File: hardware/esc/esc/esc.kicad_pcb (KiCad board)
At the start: 4 copper layers, 40.2 x 42.5 mm, 189 parts, among them J1 JST SH 1.0mm, Q1 Q_NMOS, Q10 Q_NMOS, Q11 Q_NMOS, Q12 Q_NMOS, Q13 Q_NMOS, Q14 Q_NMOS, Q15 Q_NMOS, Q16 Q_NMOS, Q17 Q_NMOS, Q18 Q_NMOS, Q19 Q_NMOS, Q2 Q_NMOS, Q20 Q_NMOS, Q21 Q_NMOS, Q22 Q_NMOS, Q23 Q_NMOS, Q24 Q_NMOS, Q3 Q_NMOS, Q4 Q_NMOS, Q5 Q_NMOS, Q6 Q_NMOS, Q7 Q_NMOS, Q8 Q_NMOS, Q9 Q_NMOS, U1 NSG2065Q, U10 TLV76733DRVR, U11 LMR51420YDDCR, U2 AT32F421G8U7, U3 INA180B2, U4 AT32F421G8U7, U5 NSG2065Q, U6 AT32F421G8U7, U7 NSG2065Q, U8 AT32F421G8U7, U9 NSG2065Q

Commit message: ESC Layout try 1
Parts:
- C15, C16, C17, C28, C29, C30, C31, C4, C42, C43, C44, C45, C5, C56, C57, C58, C59, C6, C60, C7, FB1, FB2, FB3, FB4, R18, R19, R22, R23, R25, R26, R42, R43, R45, R46, R62, R63, R65, R66, R7, R8, TP1, TP2, TP3, TP4, TP5, TP6, TP7, TP8, U1, U10, U2, U4, U5, U6, U7, U8, U9: moved to B.Cu
- moved U10 111.7 mm to (40.1, 38.9), turned to 180 degrees
- moved C60 109.1 mm to (41.9, 33.4)
- moved C59 108.2 mm to (41.9, 35.4)
- moved U2 108.1 mm to (32.2, 27.9), turned to 90 degrees
- moved R19 108.0 mm to (26.4, 23.3), turned to -90 degrees
- moved R20 107.7 mm to (32.1, 34.1), turned to -90 degrees
- moved R8 106.8 mm to (35.4, 27.4), turned to -90 degrees
- moved C57 106.4 mm to (39.3, 36.2), turned to 90 degrees
- moved R18 105.4 mm to (27.9, 23.3), turned to 90 degrees
- moved D1 104.7 mm to (34.2, 33.7)
- moved C58 104.1 mm to (41.9, 37.1)
- moved TP1 102.0 mm to (35.0, 25.0), turned to 180 degrees
- moved TP2 100.8 mm to (35.1, 30.7), turned to 180 degrees
- moved C6 100.5 mm to (29.5, 23.3), turned to 90 degrees
- moved C7 100.3 mm to (31.0, 23.3), turned to 90 degrees
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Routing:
- net +BATT: track 135.0 -> 50.7 mm, vias 8 -> 0
- net GND: track 128.2 -> 93.1 mm, vias 16 -> 0
- net /CURR_SENSE: track 26.0 -> 0.00 mm, vias 1 -> 0
- net /ESC2/FloatB: track 26.3 -> 3.16 mm, vias 1 -> 0
- net /VBAT: track 21.1 -> 0.00 mm, vias 1 -> 0
- net +3.3V: track 0.00 -> 17.1 mm
- net /ESC1/FloatB: track 19.2 -> 3.18 mm, vias 1 -> 0
- net /ESC1/FloatC: track 19.0 -> 2.99 mm, vias 1 -> 0
- net /ESC4/FloatB: track 18.2 -> 2.83 mm, vias 1 -> 0
- net /ESC3/FloatB: track 19.0 -> 4.14 mm
- net /ESC4/FloatA: track 17.9 -> 3.18 mm, vias 1 -> 0
- net /ESC3/FloatC: track 23.6 -> 11.1 mm
- net Net-(Q1-PadG): track 12.2 -> 0.04 mm, vias 2 -> 0
- net Net-(Q3-PadG): track 12.2 -> 0.00 mm, vias 2 -> 0
- net Net-(Q5-PadG): track 12.1 -> 0.00 mm, vias 2 -> 0
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
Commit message: journal for 2nd april
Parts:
- moved FB4 0.60 mm to (47.7, 38.3)
- moved R65 0.60 mm to (44.4, 38.3)
- moved C45 0.60 mm to (45.9, 38.3)
- moved R46 0.05 mm to (36.4, 27.4)
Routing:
- net /CURR_SENSE: track 0.00 -> 34.8 mm, vias 0 -> 2
- net +3.3V: track 17.1 -> 47.0 mm, vias 0 -> 1
- net Net-(Q9-PadG): track 0.00 -> 20.7 mm
- net Net-(Q3-PadG): track 0.00 -> 20.4 mm
- net /ESC4/FloatA: track 3.18 -> 22.3 mm
- net Net-(Q7-PadG): track 0.00 -> 15.8 mm, vias 0 -> 2
- net /VBAT: track 0.00 -> 15.6 mm
- net Net-(Q5-PadG): track 0.00 -> 14.5 mm
- net Net-(Q11-PadG): track 0.00 -> 14.4 mm
- net +8V: track 7.09 -> 20.7 mm
- net Net-(Q13-PadG): track 0.00 -> 13.3 mm
- net /ESC4/FloatB: track 2.83 -> 15.9 mm
- net Net-(Q1-PadG): track 0.04 -> 12.8 mm, vias 0 -> 2
- net /ESC2/VOLT_SENSE: track 0.00 -> 12.3 mm
- net Net-(Q17-PadG): track 0.00 -> 11.4 mm, vias 0 -> 2
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
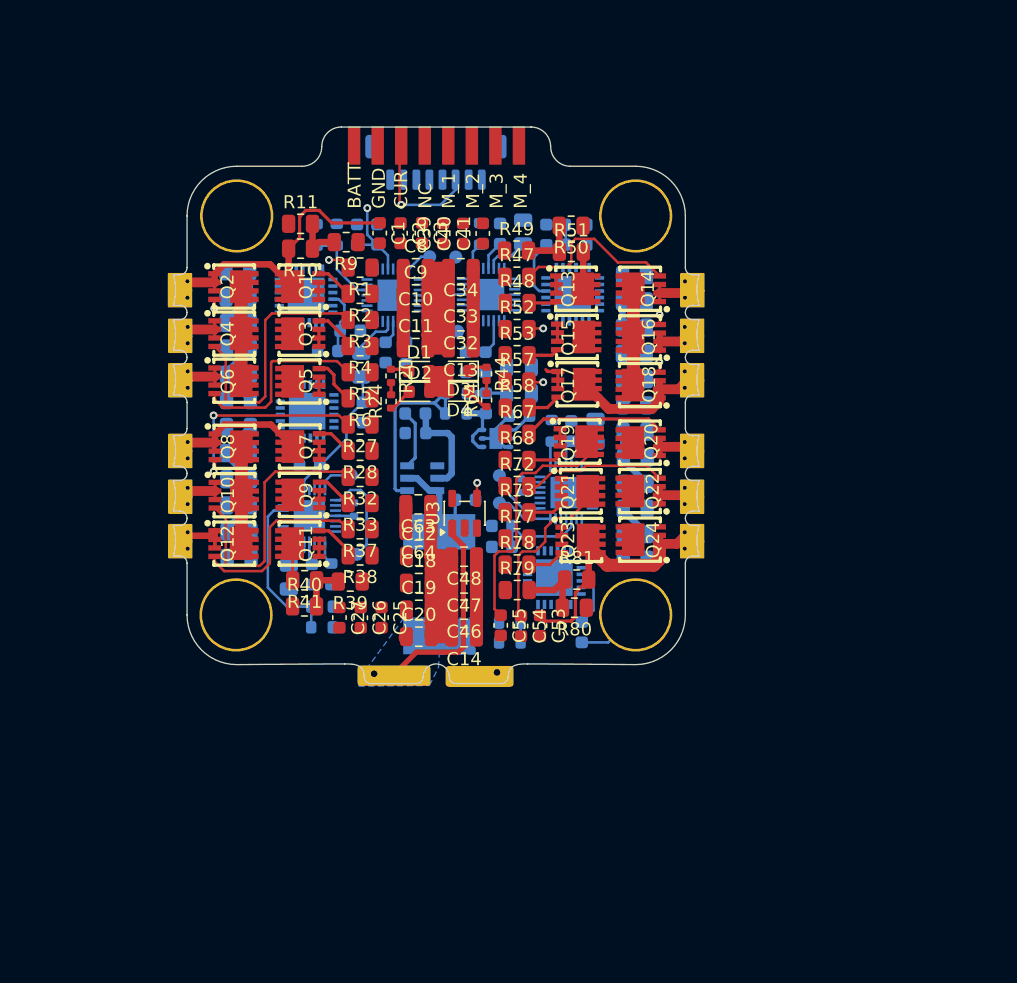
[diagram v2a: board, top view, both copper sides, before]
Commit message: redo layout and new board outline
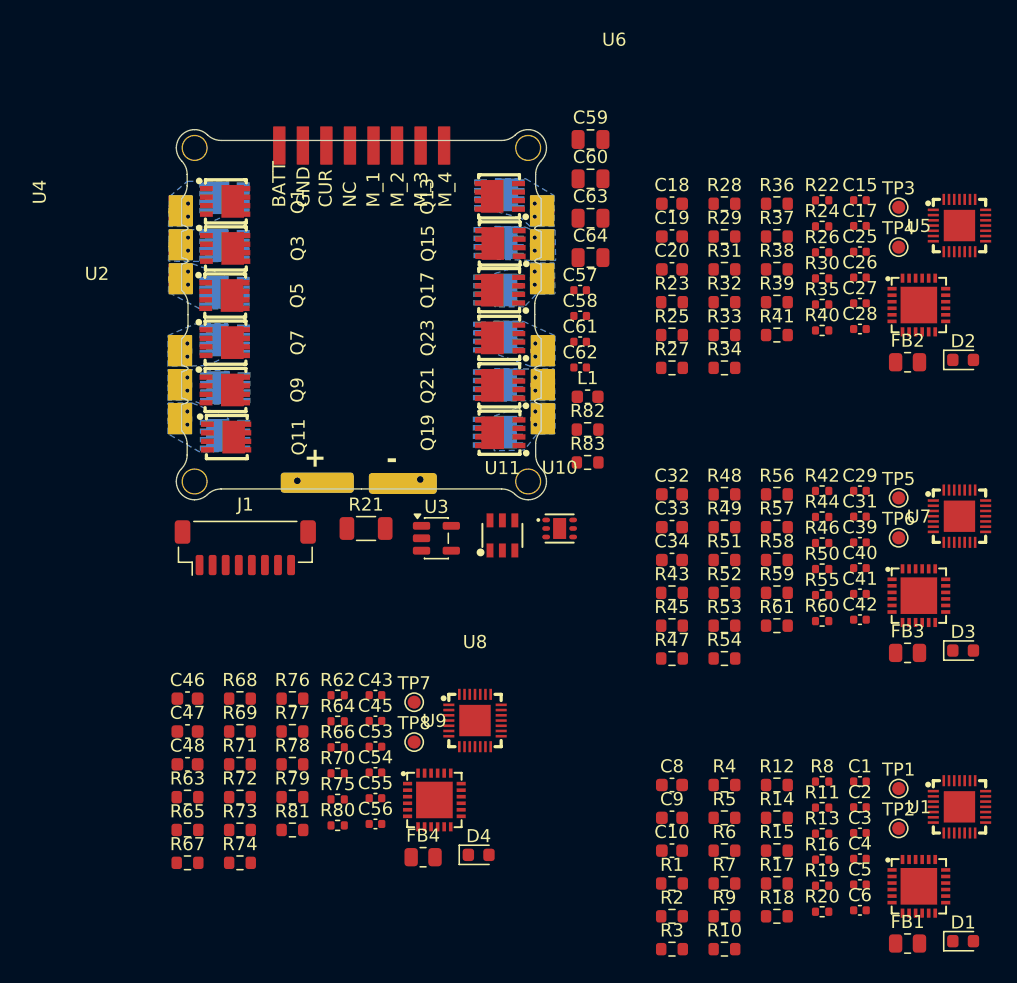
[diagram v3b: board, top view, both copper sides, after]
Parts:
- removed C11, C12, C13, C14: 22uF, Capacitor_SMD:C_0805_2012Metric
- removed C16, C30, C44, C7: 100nF, Capacitor_SMD:C_0603_1608Metric
- C1, C2, C25, C26, C27, C3, C39, C40, C41, C53, C54, C55: footprint Capacitor_SMD:C_0603_1608Metric -> Capacitor_SMD:C_0402_1005Metric
- C10, C18, C19, C20, C32, C33, C34, C46, C47, C48, C8, C9: value 22uF -> 10uF; footprint Capacitor_SMD:C_0805_2012Metric -> Capacitor_SMD:C_0603_1608Metric
- C15, C17, C28, C29, C31, C4, C42, C43, C45, C5, C56, C57, C58, C6, C61, C62: footprint Capacitor_SMD:C_0603_1608Metric -> Capacitor_SMD:C_0402_1005Metric; moved to F.Cu
- C59, C60, FB1, FB2, FB3, FB4, J1, L1, R18, R23, R25, R26, R43, R45, R46, R63, R65, R66, R7, R8, R82, R83, TP1, TP2, TP3, TP4, TP5, TP6, TP7, TP8, U1, U10, U11, U2, U4, U5, U6, U7, U8, U9: moved to F.Cu
- Q10, Q12, Q14, Q16, Q18, Q2, Q20, Q22, Q24, Q4, Q6, Q8: moved to B.Cu
- R1, R10, R2, R27, R28, R3, R32, R33, R37, R38, R39, R4, R41, R47, R48, R49, R5, R51, R52, R53, R57, R58, R6, R67, R68, R72, R73, R77, R78, R79, R81, R9: footprint Resistor_SMD:R_0805_2012Metric -> Resistor_SMD:R_0603_1608Metric
- R11, R40, R50, R80: footprint Resistor_SMD:R_0805_2012Metric -> Resistor_SMD:R_0402_1005Metric
- R12, R14, R15, R17, R29, R31, R34, R36, R54, R56, R59, R61, R69, R71, R74, R76: footprint Resistor_SMD:R_0805_2012Metric -> Resistor_SMD:R_0603_1608Metric; moved to F.Cu
- R13, R16, R30, R35, R55, R60, R70, R75: footprint Resistor_SMD:R_0805_2012Metric -> Resistor_SMD:R_0402_1005Metric; moved to F.Cu
- R19, R22, R42, R62: footprint Resistor_SMD:R_0603_1608Metric -> Resistor_SMD:R_0402_1005Metric; moved to F.Cu
- R21: footprint 3920:RES_3920R_1L00x_BRN -> Resistor_SMD:R_1206_3216Metric; moved to F.Cu
- moved U1 65.1 mm to (72.4, 73.1), turned to 0 degrees
- moved C6 64.4 mm to (67.9, 74.9), turned to 0 degrees
- moved R19 63.0 mm to (65.0, 73.1), turned to 0 degrees
- moved R10 62.6 mm to (57.6, 77.9), turned to 0 degrees
- moved R18 62.0 mm to (61.6, 75.4), turned to 0 degrees
- moved R13 62.0 mm to (65.0, 69.1)
- moved FB1 60.8 mm to (71.6, 77.5), turned to 0 degrees
- moved D1 60.3 mm to (75.8, 77.3)
- moved R11 59.9 mm to (65.0, 67.1)
- moved R9 59.1 mm to (57.6, 75.4), turned to 0 degrees
- moved U2 58.3 mm to (75.5, 67.0), turned to 0 degrees
- moved R17 58.0 mm to (61.6, 72.9), turned to 0 degrees
- moved R14 57.3 mm to (61.6, 67.9), turned to 0 degrees
- moved R16 56.8 mm to (65.0, 71.1)
- moved C3 56.8 mm to (67.9, 69.0), turned to 0 degrees
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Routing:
- net GND: track 97.4 -> 0.00 mm
- net +BATT: track 50.7 -> 0.00 mm
- net +3.3V: track 47.0 -> 0.00 mm, vias 1 -> 0
- net /CURR_SENSE: track 34.8 -> 0.00 mm, vias 2 -> 0
- net /ESC1/FloatA: track 23.2 -> 0.00 mm
- net /ESC4/FloatA: track 22.3 -> 0.00 mm
- net /ESC4/FloatC: track 21.1 -> 0.00 mm
- net Net-(Q9-PadG): track 20.7 -> 0.00 mm
- net +8V: track 20.7 -> 0.00 mm
- net Net-(Q3-PadG): track 20.4 -> 0.00 mm
- net /ESC4/FloatB: track 15.9 -> 0.00 mm
- net Net-(Q7-PadG): track 15.8 -> 0.00 mm, vias 2 -> 0
- net /VBAT: track 15.6 -> 0.00 mm
- net Net-(Q5-PadG): track 14.5 -> 0.00 mm
- net Net-(Q11-PadG): track 14.4 -> 0.00 mm
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- added copper zone on B.Cu, net /ESC1/FloatA
- added copper zone on B.Cu, net /ESC1/FloatB
- added copper zone on B.Cu, net /ESC1/FloatC
- added copper zone on B.Cu, net /ESC2/FloatA
- added copper zone on B.Cu, net /ESC2/FloatB
- added copper zone on B.Cu, net /ESC2/FloatC
- added copper zone on B.Cu, net /ESC3/FloatA
- added copper zone on B.Cu, net /ESC3/FloatB
- added copper zone on B.Cu, net /ESC3/FloatC
- added copper zone on B.Cu, net /ESC4/FloatA
- added copper zone on B.Cu, net /ESC4/FloatB
- added copper zone on B.Cu, net /ESC4/FloatC
- removed copper zone on B.Cu, net /VBAT
- removed copper zone on In1.Cu, net GND
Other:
- board size 40.2 x 42.5 mm -> 28.3 x 28.3 mm

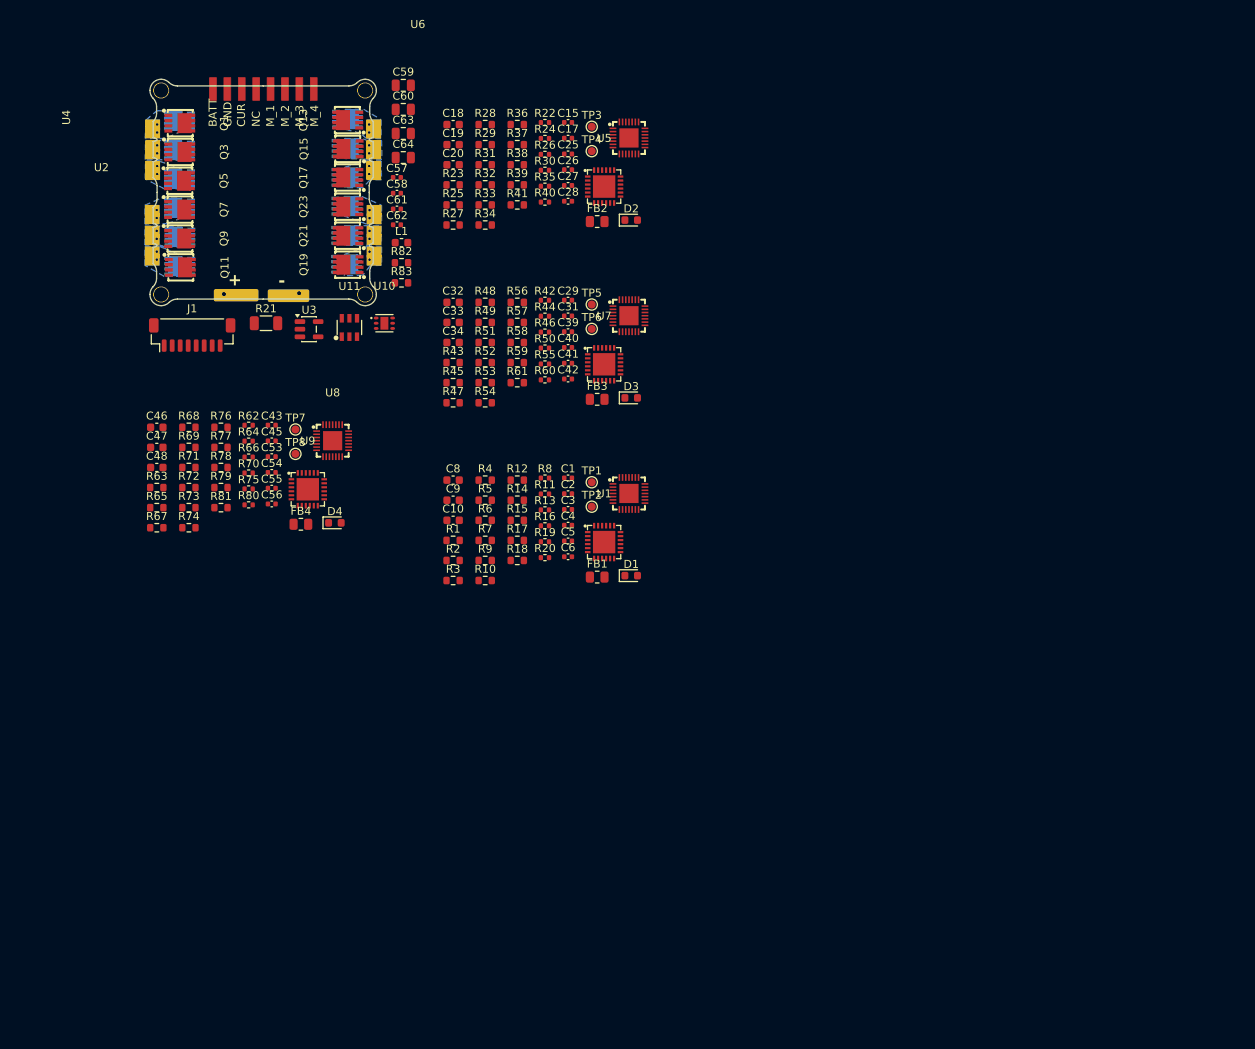
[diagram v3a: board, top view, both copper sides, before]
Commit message: board pcb + res arrays
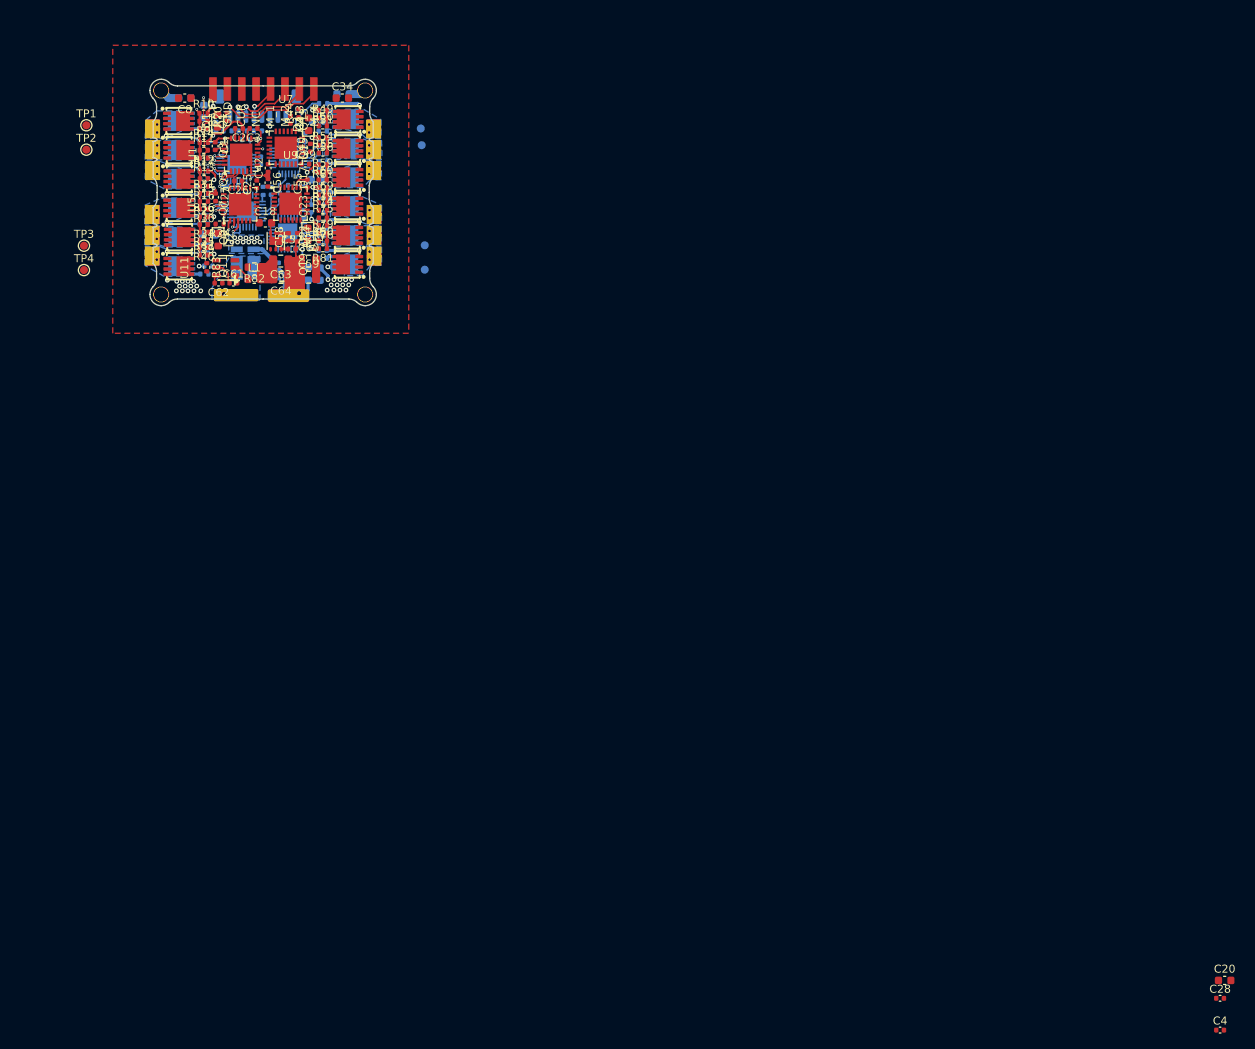
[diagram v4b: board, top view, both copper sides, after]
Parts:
- removed FB1, FB2, FB3, FB4: FerriteBead_Small, Resistor_SMD:R_0805_2012Metric
- removed R18, R23, R63: 10k, Resistor_SMD:R_0603_1608Metric
- removed R19, R22, R62: 100k, Resistor_SMD:R_0402_1005Metric
- C10, C15, C17, C19, C29, C31, C32, C33, C43, C45, C46, C47, C48, C5, C53, C54, C6, C9, J1, R26, R42, R46, R66, R8, TP5, TP6, TP7, TP8, U2, U3, U4, U6, U8: moved to B.Cu
- R1, R2, R27, R28, R3, R32, R33, R37, R38, R4, R47, R48, R5, R52, R53, R57, R58, R6, R67, R68, R72, R73, R77, R78: value 20R -> 22R; footprint Resistor_SMD:R_0603_1608Metric -> Resistor_SMD:R_0402_1005Metric; moved to B.Cu
- R10, R12, R14, R15, R17, R29, R31, R34, R36, R39, R41, R49, R51, R54, R56, R59, R61, R69, R71, R74, R76, R79, R81, R83, R9: footprint Resistor_SMD:R_0603_1608Metric -> Resistor_SMD:R_0402_1005Metric
- R21: value 0.4mR -> 0.5m; footprint Resistor_SMD:R_1206_3216Metric -> bvn-z-r0005-1.0:BVNZR000510; moved to B.Cu
- R25, R43, R45, R65, R7: footprint Resistor_SMD:R_0603_1608Metric -> Resistor_SMD:R_0402_1005Metric; moved to B.Cu
- moved C20 140.3 mm to (150.0, 127.9)
- moved C28 128.7 mm to (149.4, 130.1)
- moved C4 103.1 mm to (149.4, 134.1)
- moved TP1 77.3 mm to (7.70, 21.0)
- moved TP2 77.3 mm to (7.70, 24.1)
- moved D1 76.8 mm to (24.1, 20.4), turned to 90 degrees
- moved R10 68.2 mm to (22.4, 19.5)
- moved R20 67.9 mm to (25.3, 19.9), turned to 90 degrees
- moved U1 66.4 mm to (27.1, 24.7), turned to 90 degrees
- moved C6 65.6 mm to (22.4, 27.7), turned to 180 degrees
- moved R9 65.2 mm to (22.4, 20.5), turned to 180 degrees
- moved TP3 65.2 mm to (7.40, 36.0)
- moved TP4 65.2 mm to (7.40, 39.1)
- moved U2 64.0 mm to (26.5, 25.9), turned to 180 degrees
- moved C10 62.5 mm to (20.0, 17.6), turned to 180 degrees
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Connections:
- U2 pad 12: /ESC1/VOLT_SENSE -> unconnected-(U2-PA6-Pad12)
- U2 pad 5: Net-(U2-VDDA) -> +3.3V
- U4 pad 12: /ESC2/VOLT_SENSE -> unconnected-(U4-PA6-Pad12)
- U4 pad 5: Net-(U4-VDDA) -> +3.3V
- U6 pad 5: Net-(U6-VDDA) -> +3.3V
- U8 pad 12: /ESC4/VOLT_SENSE -> unconnected-(U8-PA6-Pad12)
- U8 pad 5: Net-(U8-VDDA) -> +3.3V
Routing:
- net GND: track 0.00 -> 57.8 mm, vias 0 -> 1
- net /ESC1/BEMF_COM: track 0.00 -> 25.5 mm, vias 0 -> 2
- net /ESC1/FloatC: track 0.00 -> 20.4 mm, vias 0 -> 2
- net /CURR_SENSE: track 0.00 -> 20.4 mm, vias 0 -> 2
- net /ESC1/FloatA: track 0.00 -> 15.9 mm, vias 0 -> 2
- net +8V: track 0.00 -> 15.6 mm
- net /ESC1/BEMF_B: track 0.00 -> 15.6 mm, vias 0 -> 2
- net /ESC1/FloatB: track 0.00 -> 15.2 mm, vias 0 -> 1
- net /ESC1/BEMF_A: track 0.00 -> 14.5 mm, vias 0 -> 2
- net /dshot_4: track 0.00 -> 13.9 mm, vias 0 -> 1
- net +BATT: track 0.00 -> 13.2 mm, vias 0 -> 37
- net /ESC1/BEMF_C: track 0.00 -> 11.3 mm, vias 0 -> 2
- net +3.3V: track 0.00 -> 11.1 mm
- net /dshot_3: track 0.00 -> 10.8 mm, vias 0 -> 1
- net /ESC4/FloatA: track 0.00 -> 10.8 mm, vias 0 -> 1
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- added copper zone on B.Cu, net +BATT
- added copper zone on F.Cu, net +BATT
- added copper zone on In2.Cu, net +BATT
- added copper zone on B.Cu, net /VBAT
- added copper zone on B.Cu, net GND
- added copper zone on In1.Cu, net GND
